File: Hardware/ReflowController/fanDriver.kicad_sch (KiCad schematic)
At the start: 12 parts, among them U5 TB67H400AFNG

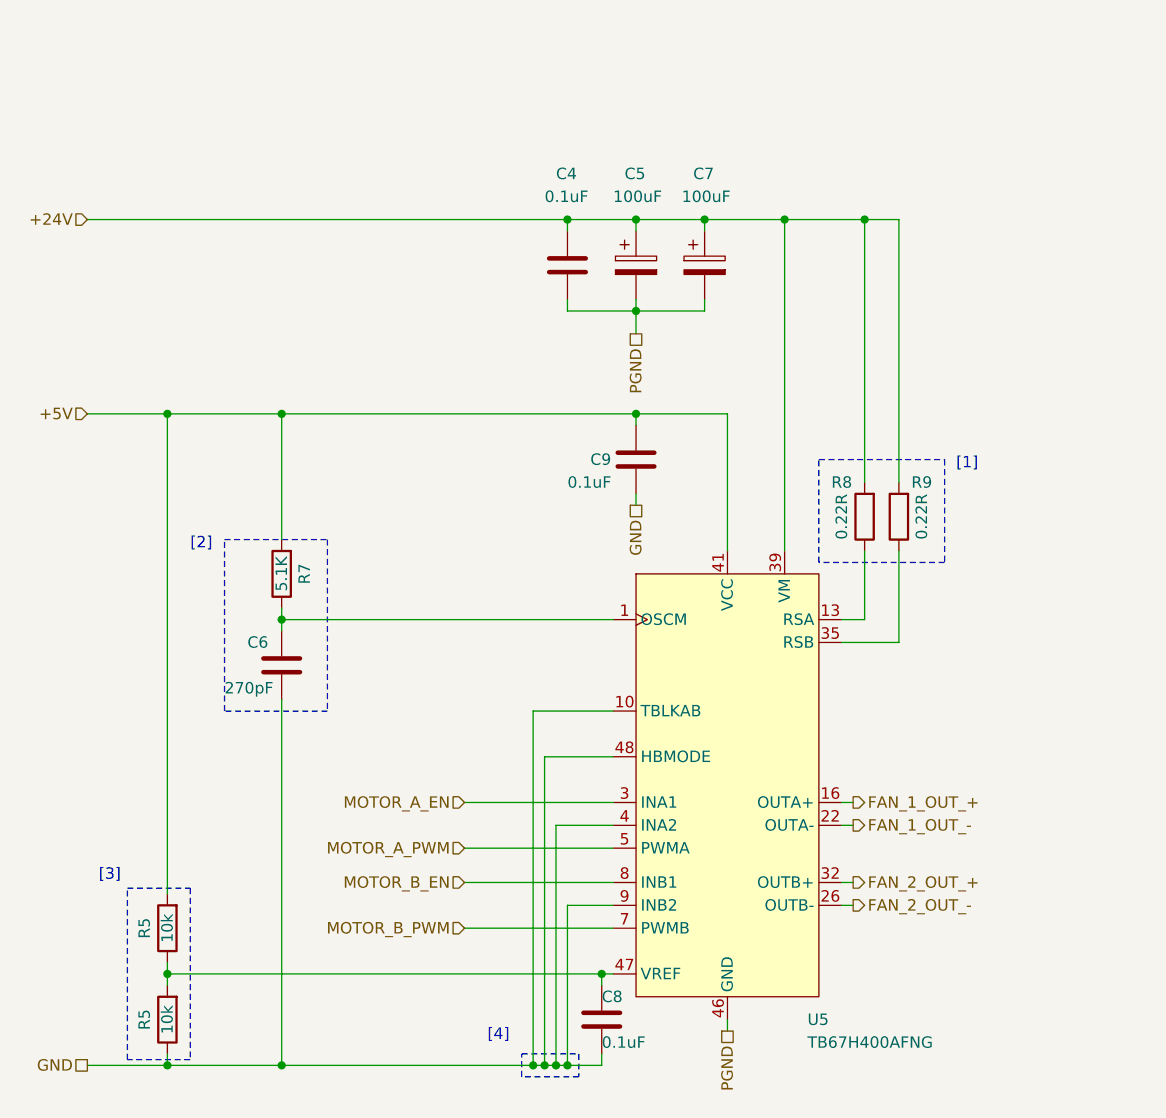
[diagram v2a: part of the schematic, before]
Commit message: Finished the desing of the PSUand started with the PCB TODO: missing fuse find a solution
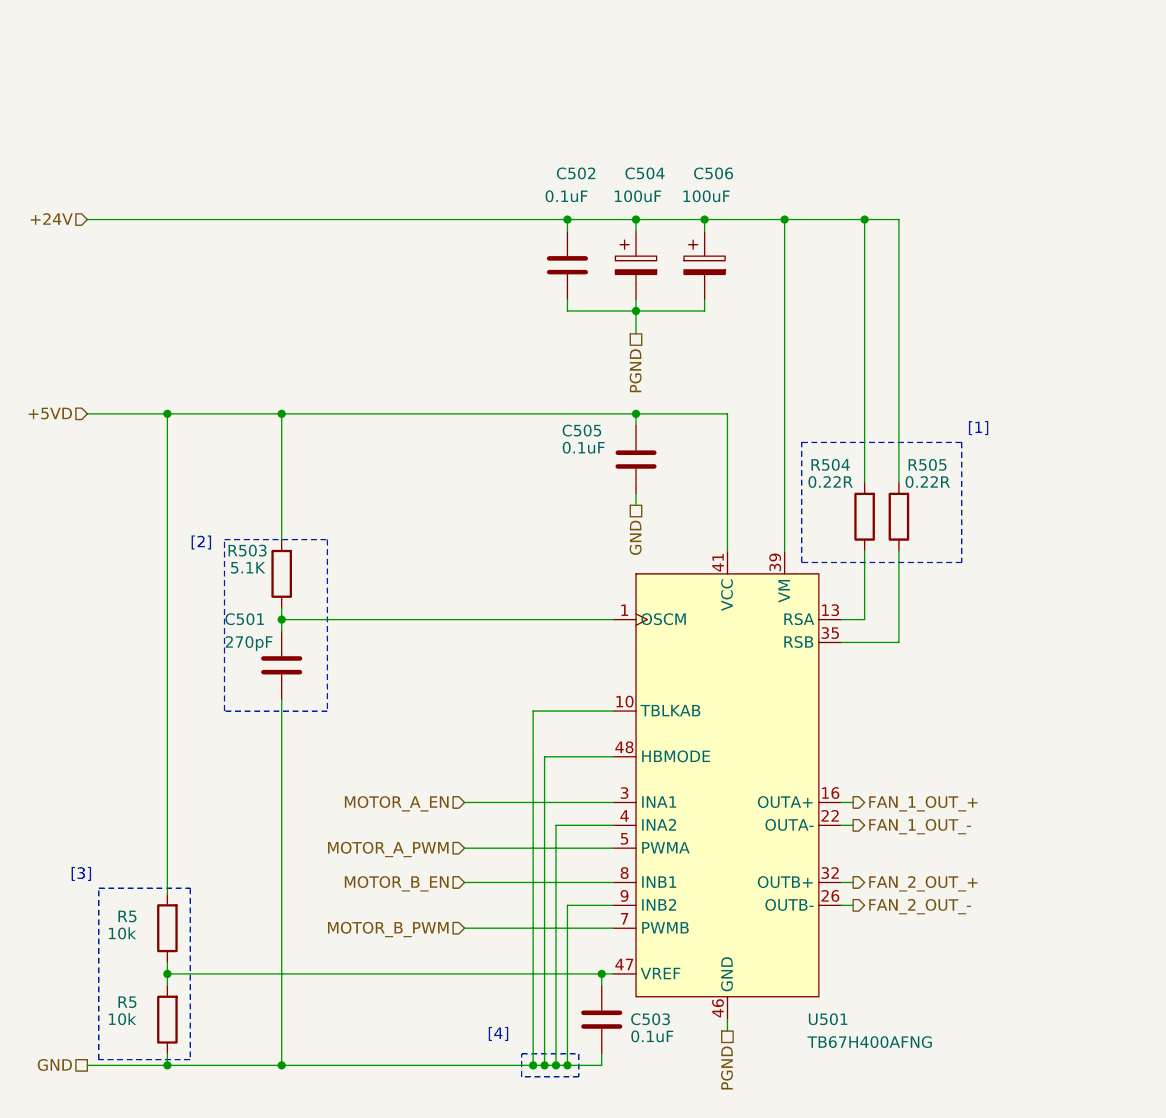
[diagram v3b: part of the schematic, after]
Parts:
- renumbered C6 to C501, C4 to C502, C8 to C503, C5 to C504, C9 to C505, C7 to C506, R7 to R503, R8 to R504, R9 to R505, U5 to U501
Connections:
- net +5V renamed +5VD
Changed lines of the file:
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@@
     (fill (type none))
   )
-  (rectangle (start 80.645 122.555) (end 87.63 141.605)
+  (rectangle (start 77.47 122.555) (end 87.63 141.605)
     (stroke (width 0) (type dot))
     (fill (type none))
   )
-  (rectangle (start 157.48 74.93) (end 171.45 86.36)
+  (rectangle (start 155.575 73.025) (end 173.355 86.36)
     (stroke (width 0) (type dot))
     (fill (type none))
@@
     (effects (font (size 1.27 1.27)) (justify left bottom))
   )
-  (text "[3]" (at 77.47 121.92 0)
+  (text "[3]" (at 74.295 121.92 0)
     (effects (font (size 1.27 1.27)) (justify left bottom))
   )
@@
     (effects (font (size 1.27 1.27)) (justify left bottom))
   )
-  (text "[1]" (at 172.72 76.2 0)
+  (text "[1]" (at 173.99 72.39 0)
     (effects (font (size 1.27 1.27)) (justify left bottom))
   )
@@
     (effects (font (size 1.27 1.27)) (justify right))
   )
-  (hierarchical_label "+5V" (shape input) (at 76.2 69.85 180) (fields_autoplaced)
+  (hierarchical_label "+5VD" (shape input) (at 76.2 69.85 180) (fields_autoplaced)
     (effects (font (size 1.27 1.27)) (justify right))
   )
@@
   (symbol (lib_id "350_power_driver_motor_dc:TB67H400AFNG,EL") (at 147.32 113.03 0) (unit 1)
     (in_bom yes) (on_board yes) (dnp no)
-    (property "Reference" "U5" (at 156.21 137.16 0)
+    (property "Reference" "U501" (at 156.21 137.16 0)
       (effects (font (size 1.27 1.27)) (justify left))
     )
@@
       (project "ReflowController"
         (path "/2394cc2a-b9b0-4c0b-be11-1fc6085b0d5c/88b069ca-209a-441b-9ebc-a973d3ca8ace"
-          (reference "U5") (unit 1)
+          (reference "U501") (unit 1)
         )
       )
@@
   (symbol (lib_id "Device:C_Polarized") (at 144.78 53.34 0) (unit 1)
     (in_bom yes) (on_board yes) (dnp no)
-    (property "Reference" "C7" (at 143.51 43.18 0)
+    (property "Reference" "C506" (at 143.51 43.18 0)
       (effects (font (size 1.27 1.27)) (justify left))
     )
@@
       (project "ReflowController"
         (path "/2394cc2a-b9b0-4c0b-be11-1fc6085b0d5c/88b069ca-209a-441b-9ebc-a973d3ca8ace"
-          (reference "C7") (unit 1)
+          (reference "C506") (unit 1)
         )
       )
@@
   (symbol (lib_id "Device:C") (at 137.16 74.93 0) (unit 1)
     (in_bom yes) (on_board yes) (dnp no)
-    (property "Reference" "C9" (at 132.08 74.93 0)
-      (effects (font (size 1.27 1.27)) (justify left))
-    )
-    (property "Value" "0.1uF" (at 129.54 77.47 0)
+    (property "Reference" "C505" (at 128.905 71.755 0)
+      (effects (font (size 1.27 1.27)) (justify left))
+    )
+    (property "Value" "0.1uF" (at 128.905 73.66 0)
       (effects (font (size 1.27 1.27)) (justify left))
     )
@@
       (project "ReflowController"
         (path "/2394cc2a-b9b0-4c0b-be11-1fc6085b0d5c/88b069ca-209a-441b-9ebc-a973d3ca8ace"
-          (reference "C9") (unit 1)
+          (reference "C505") (unit 1)
         )
       )
@@
   (symbol (lib_id "Device:R") (at 85.09 127 180) (unit 1)
     (in_bom yes) (on_board yes) (dnp no)
-    (property "Reference" "R5" (at 82.55 127 90)
-      (effects (font (size 1.27 1.27)))
-    )
-    (property "Value" "10k" (at 85.09 127 90)
+    (property "Reference" "R5" (at 80.645 125.73 0)
+      (effects (font (size 1.27 1.27)))
+    )
+    (property "Value" "10k" (at 80.01 127.635 0)
       (effects (font (size 1.27 1.27)))
     )
@@
         )
         (path "/2394cc2a-b9b0-4c0b-be11-1fc6085b0d5c/88b069ca-209a-441b-9ebc-a973d3ca8ace"
-          (reference "R5") (unit 1)
+          (reference "R501") (unit 1)
         )
       )
@@
   (symbol (lib_id "Device:C") (at 97.79 97.79 0) (unit 1)
     (in_bom yes) (on_board yes) (dnp no)
-    (property "Reference" "C6" (at 93.98 95.25 0)
-      (effects (font (size 1.27 1.27)) (justify left))
-    )
-    (property "Value" "270pF" (at 91.44 100.33 0)
+    (property "Reference" "C501" (at 91.44 92.71 0)
+      (effects (font (size 1.27 1.27)) (justify left))
+    )
+    (property "Value" "270pF" (at 91.44 95.25 0)
       (effects (font (size 1.27 1.27)) (justify left))
     )
@@
       (project "ReflowController"
         (path "/2394cc2a-b9b0-4c0b-be11-1fc6085b0d5c/88b069ca-209a-441b-9ebc-a973d3ca8ace"
-          (reference "C6") (unit 1)
+          (reference "C501") (unit 1)
         )
       )
@@
   (symbol (lib_id "Device:R") (at 162.56 81.28 180) (unit 1)
     (in_bom yes) (on_board yes) (dnp no)
-    (property "Reference" "R8" (at 160.02 77.47 0)
-      (effects (font (size 1.27 1.27)))
-    )
-    (property "Value" "0.22R" (at 160.02 81.28 90)
+    (property "Reference" "R504" (at 158.75 75.565 0)
+      (effects (font (size 1.27 1.27)))
+    )
+    (property "Value" "0.22R" (at 158.75 77.47 0)
       (effects (font (size 1.27 1.27)))
     )
@@
       (project "ReflowController"
         (path "/2394cc2a-b9b0-4c0b-be11-1fc6085b0d5c/88b069ca-209a-441b-9ebc-a973d3ca8ace"
-          (reference "R8") (unit 1)
+          (reference "R504") (unit 1)
         )
       )
@@
   (symbol (lib_id "Device:R") (at 97.79 87.63 180) (unit 1)
     (in_bom yes) (on_board yes) (dnp no)
-    (property "Reference" "R7" (at 100.33 87.63 90)
-      (effects (font (size 1.27 1.27)))
-    )
-    (property "Value" "5.1K" (at 97.79 87.63 90)
+    (property "Reference" "R503" (at 93.98 85.09 0)
+      (effects (font (size 1.27 1.27)))
+    )
+    (property "Value" "5.1K" (at 93.98 86.995 0)
       (effects (font (size 1.27 1.27)))
     )
@@
       (project "ReflowController"
         (path "/2394cc2a-b9b0-4c0b-be11-1fc6085b0d5c/88b069ca-209a-441b-9ebc-a973d3ca8ace"
-          (reference "R7") (unit 1)
+          (reference "R503") (unit 1)
         )
       )
@@
   (symbol (lib_id "Device:R") (at 166.37 81.28 180) (unit 1)
     (in_bom yes) (on_board yes) (dnp no)
-    (property "Reference" "R9" (at 168.91 77.47 0)
-      (effects (font (size 1.27 1.27)))
-    )
-    (property "Value" "0.22R" (at 168.91 81.28 90)
+    (property "Reference" "R505" (at 169.545 75.565 0)
+      (effects (font (size 1.27 1.27)))
+    )
+    (property "Value" "0.22R" (at 169.545 77.47 0)
       (effects (font (size 1.27 1.27)))
     )
@@
       (project "ReflowController"
         (path "/2394cc2a-b9b0-4c0b-be11-1fc6085b0d5c/88b069ca-209a-441b-9ebc-a973d3ca8ace"
-          (reference "R9") (unit 1)
+          (reference "R505") (unit 1)
         )
       )
@@
   (symbol (lib_id "Device:C_Polarized") (at 137.16 53.34 0) (unit 1)
     (in_bom yes) (on_board yes) (dnp no)
-    (property "Reference" "C5" (at 135.89 43.18 0)
+    (property "Reference" "C504" (at 135.89 43.18 0)
       (effects (font (size 1.27 1.27)) (justify left))
     )
@@
       (project "ReflowController"
         (path "/2394cc2a-b9b0-4c0b-be11-1fc6085b0d5c/88b069ca-209a-441b-9ebc-a973d3ca8ace"
-          (reference "C5") (unit 1)
+          (reference "C504") (unit 1)
         )
       )
@@
   (symbol (lib_id "Device:R") (at 85.09 137.16 180) (unit 1)
     (in_bom yes) (on_board yes) (dnp no)
-    (property "Reference" "R5" (at 82.55 137.16 90)
-      (effects (font (size 1.27 1.27)))
-    )
-    (property "Value" "10k" (at 85.09 137.16 90)
+    (property "Reference" "R5" (at 80.645 135.255 0)
+      (effects (font (size 1.27 1.27)))
+    )
+    (property "Value" "10k" (at 80.01 137.16 0)
       (effects (font (size 1.27 1.27)))
     )
@@
         )
         (path "/2394cc2a-b9b0-4c0b-be11-1fc6085b0d5c/88b069ca-209a-441b-9ebc-a973d3ca8ace"
-          (reference "R6") (unit 1)
+          (reference "R502") (unit 1)
         )
       )
@@
   (symbol (lib_id "Device:C") (at 129.54 53.34 0) (unit 1)
     (in_bom yes) (on_board yes) (dnp no)
-    (property "Reference" "C4" (at 128.27 43.18 0)
+    (property "Reference" "C502" (at 128.27 43.18 0)
       (effects (font (size 1.27 1.27)) (justify left))
     )
@@
       (project "ReflowController"
         (path "/2394cc2a-b9b0-4c0b-be11-1fc6085b0d5c/88b069ca-209a-441b-9ebc-a973d3ca8ace"
-          (reference "C4") (unit 1)
+          (reference "C502") (unit 1)
         )
       )
@@
   (symbol (lib_id "Device:C") (at 133.35 137.16 0) (unit 1)
     (in_bom yes) (on_board yes) (dnp no)
-    (property "Reference" "C8" (at 133.35 134.62 0)
-      (effects (font (size 1.27 1.27)) (justify left))
-    )
-    (property "Value" "0.1uF" (at 133.35 139.7 0)
+    (property "Reference" "C503" (at 136.525 137.16 0)
+      (effects (font (size 1.27 1.27)) (justify left))
+    )
+    (property "Value" "0.1uF" (at 136.525 139.065 0)
       (effects (font (size 1.27 1.27)) (justify left))
     )
@@
       (project "ReflowController"
         (path "/2394cc2a-b9b0-4c0b-be11-1fc6085b0d5c/88b069ca-209a-441b-9ebc-a973d3ca8ace"
-          (reference "C8") (unit 1)
-        )
-      )
+          (reference "C503") (unit 1)
+        )
+      )

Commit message: Made some progress on the PCB desgin for now only the main blocks are complete, thw pin connection of the mCU should be organised and Net-ties are making life much harder as you cant put them on the middle layers
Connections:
- net PGND: now also U501.PAD (GND)
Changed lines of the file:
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@@
     (pin "48")
     (pin "6")
+    (pin "PAD")
     (instances
       (project "ReflowController"
